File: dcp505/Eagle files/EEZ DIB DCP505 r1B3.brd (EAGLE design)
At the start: 160 x 95 mm, 328 parts, among them IC1 LP2951, IC10 OPA4197IDR, IC11 MC33272ADR2G, IC12 MC33274ADR2G, IC13 74HC4066PW, IC14 74AUP1G74DC.125, IC15 MCP23S17-E/SS, IC16 REF5025AIDR, IC17 DAC8552IDGKR, IC18 SN74LVC1G3157DCKR, IC19 ADS1120IPWR, IC2 SI8641BB-B-IS1, IC20 LM339D, IC21 LM211PWR, IC3 SN74LVC1G139DCUR, IC4 MC79L05, IC5 SI8641BB-B-IS1, IC6 AT24C04D-SSHM-T, IC7 TMP1075AIDGK, IC8 TL072D, IC9 MC33274ADR2G, J1 FCR7350R, J2 FCR7350B, K1 G6K-2F-5DC, Q1 IRFP250MPBF, Q10 MMBT5551, Q11 PSMN0R9-25YLC, Q12 PSMN0R9-25YLC, Q13 PSMN0R9-25YLC, Q14 2N7002, Q15 2N7002, Q16 MMBT5401, Q17 MMBT5401, Q18 2N7002, Q19 BSS84P, Q2 BCP56-16.115, Q20 BTA26-600, Q21 2N7002, Q22 MMBT5551, Q23 2N7002, Q24 2N7002, Q25 MMBT5551, Q26 MMBT5551, Q27 MMBT5401, Q28 MMBT5551, Q29 MMBT5551, Q3 BC856C, Q30 BSS84P, Q31 2N7002, Q4 BCP56-16.115, Q5 STF10P6F6, Q6 BCP56-16.115, Q7 MMBT5401, Q8 MMBT5401, Q9 MMBT5551, X1 ZL263-26DG, X2 22-05-7085, X3 39-30-3035, X4 1844249, X5 ZL263-20DG

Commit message: #26, #28, #29
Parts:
- added C76: 10n, rcl:C0805
- added Q32: 2N7002, EEZ_Lib1:SOT103P240X110-3N
- added R139: 10K, rcl:R0805
- added R140: 470R, rcl:R0805
- added R141: 100K, rcl:R0805
- C11: value 470n -> 100n; device rcl:C0805 -> rcl:C0603
- C43: value 10n -> 47n; device rcl:C0603 -> rcl:C0805
- C44: device rcl:C0603 -> rcl:C0805
- C45: value 100n -> 10n; device rcl:C0603 -> rcl:C0805
- C47, C59, C61, C63: value 1u -> 100n; device rcl:C0805 -> rcl:C0603
- C48: value 10u -> 1u; device rcl:C1206 -> rcl:C0805
- C49: value 100n -> 10u; device rcl:C0603 -> rcl:C1206
- C50: value 4u7 -> 100n; device EEZ_Lib1:EC1206 -> rcl:C0603
- C51: value 1u -> 4u7; device rcl:C0805 -> EEZ_Lib1:EC1206
- C52, C60, C62, C64: value 100n -> 1u; device rcl:C0603 -> rcl:C0805
- C53: value 3n3 -> 100n; device rcl:C0805 -> rcl:C0603
- C55: value 10n -> 3n3
- C56: value 3n3 -> 10n
- C58: value 100n -> 3n3; device rcl:C0603 -> rcl:C0805
- C66, C68: value N.C. -> 100n; device rcl:C0805 -> rcl:C0603
- C67: value 100n -> 1n; device rcl:C0603 -> rcl:C0805
- C69: value 10n -> 1n
- C70: value 10n/200V -> 10n; device rcl:C1206 -> rcl:C0805
- C71: value 2n2 -> 10n/200V; device rcl:C0805 -> rcl:C1206
- C72: value 470n -> 2n2; device rcl:C1206 -> rcl:C0805
- C73: value HHXC630ARA330MHA0G -> 470n; device EEZ_Lib1:CAPAE830X1050N -> rcl:C1206
- C74: value 10n/200V -> HHXC630ARA330MHA0G; device rcl:C1206 -> EEZ_Lib1:CAPAE830X1050N
- C75: value 10n -> 10n/200V; device rcl:C0805 -> rcl:C1206
- IC8: value TL072D -> MC33272ADR2G
- Q22: value MMBT5551 -> FMMT493TA
- Q25: value MMBT5551 -> 2N7002; device transistor:SOT23-BEC -> EEZ_Lib1:SOT103P240X110-3N
- Q27: value MMBT5401 -> MMBT5551
- Q28: value MMBT5551 -> MMBT5401
- Q30: value BSS84P -> MMBT5551; device EEZ_Lib1:SOT95P237X112-3N -> transistor:SOT23-BEC
- Q31: value 2N7002 -> BSS84P; device EEZ_Lib1:SOT103P240X110-3N -> EEZ_Lib1:SOT95P237X112-3N
- R100: value 10R -> 220R
- R101: value 10K -> 220R
- R102: value 10K -> 10R
- R103: value 470R -> 10K
- R104: value 5K1 -> 10K
- R105: value 47K -> 470R
- R106, R120: value 5K6 -> 5K1
- R107: value 330R -> 47K
- R108: value 750R -> 5K6
- R109, R114: value 1K -> 330R
- R110: value AC01000001007JA100 -> 750R; device rcl:0411/15 -> rcl:R0805
- R111: value 2K2 -> 1K
- R112: value 330R -> AC01000001007JA100; device rcl:R0805 -> rcl:0411/15
- R113: value 10K -> 2K2
- R116: value 6R8 -> 10K
- R117, R93: value 10K -> 100K
- R118: value 5K1 -> 6R2
- R122: value 1K -> 4K7
- R123: value 330R -> 5K6
- R124, R133: value 47K -> 10K
- R125: value 47K -> 1K
- R126: value 750R -> 330R
- R127: value 1K -> 47K
- R128: value 2K2 -> 47K
- R129: value 10K -> 750R
- R130, R77, R79, R84: value 10K -> 1K
- R131: value 1R -> 2K2
- R132: value 750R -> 10K
- R134: value 330R -> 1R
- R135: value 470R -> 750R
- R136: value 10K -> 47K
- R137: value 470R -> 330R
- R138: value 100K -> 470R
- R3: value 82K -> 86K6
- R59, R70: value 499K 0.1% -> 10K; device rcl:R0603 -> rcl:R0805
- R60: value 10K -> 1R
- R61: value 1R -> 0R1; device rcl:R0805 -> rcl:R1206
- R62: value 0R1 -> 0R010; device rcl:R1206 -> EEZ_Lib1:R_H2728
- R63: value 0R010 -> 10K; device EEZ_Lib1:R_H2728 -> rcl:R0805
- R64, R74: value 10K -> 499K 0.1%; device rcl:R0805 -> rcl:R0603
- R65: value 1K 0.1% -> 1K; device rcl:R0603 -> rcl:R0805
- R68: value 1K -> 40K2 0.1%; device rcl:R0805 -> rcl:R0603
- R69: value 40K2 0.1% -> 10K; device rcl:R0603 -> rcl:R0805
- R72: value 10K -> 0R010; device rcl:R0805 -> EEZ_Lib1:R_H2728
- R73: value 0R010 -> 1K 0.1%; device EEZ_Lib1:R_H2728 -> rcl:R0603
- R75, R81: value 100R -> 10K
- R76, R86: value 1K -> 1M
- R78, R82: value 1K -> 100R
- R88: value 100K -> 1K
- R89: value 270R -> 10K
- R90: value 47K -> 100K
- R91: value 100K -> 270R
- R92: value 470R -> 47K
- R94, R98, R99: value 220R -> 470R
- R95: value 220R -> 10K
- R96, R97: value 470R -> 220R
- moved R107 151.5 mm to (154.1, 27.2), turned to 90 degrees
- moved R136 134.0 mm to (23.0, 71.8), turned to 180 degrees
- moved Q30 133.1 mm to (23.0, 62.7), turned to 180 degrees
- moved R123 131.9 mm to (149.4, 14.3), turned to 180 degrees
- moved R124 130.7 mm to (150.2, 27.2), turned to 270 degrees
- moved Q31 126.4 mm to (142.4, 3.94), turned to 270 degrees
- moved R92 124.7 mm to (129.7, 33.5), turned to 0 degrees
- moved R91 113.3 mm to (12.8, 31.8), turned to 90 degrees
- moved R94 111.3 mm to (12.5, 76.3), turned to 180 degrees
- moved R98 110.6 mm to (11.8, 69.5), turned to 270 degrees
- moved R103 110.3 mm to (156.1, 27.2)
- moved R89 110.3 mm to (107.1, 89.0), turned to 270 degrees
- moved R96 108.9 mm to (110.7, 23.9), turned to 0 degrees
- moved R105 108.4 mm to (47.4, 45.9), turned to 270 degrees
- moved R97 105.9 mm to (110.7, 27.9), turned to 0 degrees
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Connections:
- new net !OVP_FAULT: D23.C, IC15.25, Q25.3, R122.2
- net !DP_DRIVE: now also R95.1; no longer R93.1
- net !FAULT_OUT: now also Q31.2, R89.2; no longer Q30.2, R87.2
- net !OVP_EN: now also Q26.B; no longer Q25.B
- net !SET_DP: now also R93.2; no longer R91.2
- net +5V: now also C46.1, C47.2, C60.2, R106.2, R120.2, R132.2, R138.2, R139.1, R89.1, R93.1; no longer C45.1, C46.2, C58.2, R104.2, R118.2, R129.2, R135.2, R136.1, R87.1, R91.1
- net +VREF: now also C51.+, C53.2, C63.2, R81.2, R87.2; no longer C50.+, C52.2, C62.2, R78.2, R85.2
- net AUX_IN: now also C56.2, R98.1; no longer C55.2, R96.1
- net AUX_USET_SW: now also R92.2; no longer R90.2
- net CC_ACTIVE: now also R120.1, R123.2; no longer R118.1, R120.2
- net CC_LED: now also R114.2; no longer R112.2
- net CV_ACTIVE: now also R106.1, R108.2; no longer R104.1, R106.2
- net CV_LED: now also R109.1; no longer R107.1
- net DP_LED: now also R95.2; no longer R93.2
- net GND: now also C46.2, C47.1, C49.2, C50.1, C51.-, C52.2, C56.1, C57.2, C63.1, C64.2, C69.1, Q25.2, Q27.E, Q29.E, Q31.3, Q32.2, R113.1, R115.2, R116.2, R117.1, R118.1, R119.2, R125.2, R127.1, R136.1, R141.1, R68.1, R71.1, R74.2, R91.2, R94.1; no longer C45.2, C46.1, C47.2, C49.1, C50.-, C51.2, C52.1, C56.2, C57.1, C63.2, C64.1, Q26.E, Q28.E, Q30.3, Q31.2, R111.1, R113.2, R114.2, R115.1, R116.1, R117.2, R122.2, R124.1, R133.1, R138.1, R69.1, R70.2, R72.1, R86.1, R89.2
- net ISENSE-: now also R68.2; no longer R69.2
- net I_CTRL: now also R59.2; no longer R60.2
- net I_MON: now also R101.1; no longer R99.1
- net I_SERVO: now also R124.1; no longer R121.1
- net I_SET: now also R96.1; no longer R94.1
- net N$1: now also R67.2, R72.2S; no longer R65.2, R73.2S
- net N$105: now also R108.1; no longer R106.1
- net N$106: now also R123.1; no longer R120.1
- net N$107: now also C70.2, Q28.B, R126.1, R129.2, R131.2; no longer C69.2, Q27.B, R123.1, R126.2, R128.2
- net N$108: now also C72.2, Q28.C, R128.1, R133.2; no longer C71.2, Q27.C, R125.1, R130.2
- net N$109: now also Q30.C, R130.1; no longer Q29.C, R127.1
- net N$110: now also C76.1, Q30.B, R135.1, R137.2; no longer C75.1, Q29.B, R132.1, R134.2
- net N$111: now also C72.1, Q27.B, R127.2, R128.2; no longer C71.1, Q26.B, R124.2, R125.2
- net N$112: now also Q29.B, R133.1, R136.2; no longer Q28.B, R130.1, R133.2
- net N$113: now also C73.2, R134.2; no longer C72.2, R131.2
- net N$114: now also Q32.3, R140.1; no longer Q31.3, R137.1
- net N$118: now also R109.2; no longer R107.2
- net N$12: now also R91.1; no longer R89.1
- net N$120: now also R140.2; no longer R137.2
- net N$121: now also R94.2; no longer R92.2
- net N$14: now also Q31.1, R139.2; no longer Q30.1, R136.2
- net N$15: now also R112.2; no longer R110.2
- net N$153: now also R103.2; no longer R101.2
- net N$161: now also R124.2; no longer R121.2
- net N$17: now also R98.2, R99.1; no longer R96.2, R97.1
- net N$170: now also R107.1, R113.2; no longer R105.1, R111.2
- net N$173: now also R130.2, R131.1; no longer R127.2, R128.1
- net N$177: now also R119.1, R121.2; no longer R117.1, R119.2
- net N$18: now also R105.1; no longer R103.1
- net N$19: now also R118.2; no longer R116.2
- net N$21: now also R111.1, R117.2; no longer R109.1, R115.2
- net N$23: now also R85.2, R87.1; no longer R83.2, R85.1
- net N$24: now also Q26.C; no longer Q25.C
- net N$25: now also R138.1; no longer R135.1
- net N$28: now also C43.1, R64.2, R67.1; no longer R59.2, R65.1
- net N$29: now also R62.2; no longer R63.2
- net N$30: now also Q26.E, R125.1; no longer Q25.E, R122.1
- net N$31: now also C67.2, R104.2; no longer C66.2, R102.2
- net N$32: now also R99.2; no longer R97.2
- net N$33: now also C69.2, R110.2, R115.1; no longer C68.2, R108.2, R113.1
- net N$35: now also C43.2, R64.1, R69.2; no longer R59.1, R74.2
- net N$37: now also C44.2, R76.1; no longer C43.2
- net N$4: now also C71.1, C73.1, C74.+, Q28.E, R126.2; no longer C69.1, C72.1, C73.+, Q27.E, R123.2
- net N$40: now also R63.1; no longer R64.1
- net N$41: now also R59.1, R63.2; no longer R60.1, R64.2
- net N$42: now also R79.1, R84.2; no longer R78.1, R82.2
- net N$43: now also C45.2, R65.2, R86.1; no longer C44.2, R68.2
- net N$44: now also R70.1, R71.2; no longer R71.1, R72.2
- net N$45: now also R90.2; no longer R88.2
- net N$46: now also R114.1; no longer R112.1
- net N$47: now also R84.1, R88.2; no longer R82.1, R86.2
- net N$48: now also R82.2, R85.1; no longer R81.2, R83.1
- net N$50: now also R72.1S, R73.2; no longer R67.2, R73.1S
- net N$51: now also R62.1S; no longer R63.1S
- net N$52: now also R77.2, R81.1; no longer R76.2, R79.1
- net N$53: now also R77.1, R78.2; no longer R75.2, R76.1
- net N$54: now also R73.1, R74.1; no longer R67.1, R70.1
- net N$56: now also R61.2; no longer R62.2
- net N$57: now also R69.1; no longer R74.1
- net N$58: now also R75.2, R78.1; no longer R75.1, R77.2
- net N$59: now also R62.2S; no longer R63.2S
- net N$62: now also R82.1, R83.2; no longer R81.1, R84.2
- net N$63: now also R60.1; no longer R61.1
- net N$65: now also C44.1, R75.1, R76.2; no longer C43.1, R77.1
- net N$67: now also C45.1, R83.1, R86.2; no longer C44.1, R84.1
- net N$7: now also D15.C, R60.2, R61.1, R72.2; no longer R61.2, R63.1, R73.2
- net N$70: now also C62.2, R102.2; no longer C60.2, R100.2
- net N$71: now also C52.1; no longer C51.1
- net N$72: now also C54.2, R96.2; no longer C53.2, R94.2
- net N$73: now also C58.2, R100.2; no longer C57.2, R98.2
- net N$74: now also R65.1; no longer R68.1
- net N$8: now also R70.2; no longer R71.2
- net N$80: now also C55.2, R97.2; no longer C54.2, R95.2
- net N$81: now also C57.1, R101.2; no longer C56.1, R99.2
- net OUTF+: now also R105.2; no longer R103.2
- net OVP_FAULT: now also Q25.1, R111.2, R116.1; no longer IC15.25, R109.2, R114.1
- net PE: now also C71.2, C75.1; no longer C70.2, C74.1
- net POST_OUT-: now also C74.-, C76.2, Q30.E, R137.1; no longer C73.-, C74.2, Q29.E, R131.1
- net PREG_OUT-: now also R112.1, R72.1; no longer D15.C, R110.1, R73.1
- net PWRGOOD: no longer D23.C
- net RSENSE: now also Q32.1, R141.2; no longer Q31.1, R138.2
- net SENSE+: now also R129.1; no longer R126.1
- net SENSE-: now also R135.2; no longer R132.2
- net SENSE_ERR: now also Q29.C, R132.1; no longer Q28.C, R129.1
- net SENSE_PROT: now also Q27.C; no longer Q26.C
- net U_MON: now also R100.1, R110.1; no longer R108.1, R98.1
- net U_SERVO: now also R103.1; no longer R101.1
- net U_SET: now also R104.1, R97.1; no longer R102.1, R95.1
- net V+: now also C49.1, C50.2, C64.1, C66.2, IC12.4, R102.1, R107.2, R122.1; no longer C47.1, C49.2, C63.1, C64.2, IC12.11, R100.1, R105.2
- net V-: now also C68.2, IC12.11, R121.1; no longer C67.2, IC12.4, R119.1
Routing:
- net !OVP_FAULT: track 0.00 -> 105.0 mm, vias 0 -> 6
- net OVP_FAULT: track 116.3 -> 40.9 mm, vias 6 -> 2
- net PWRGOOD: track 94.6 -> 66.9 mm, vias 8 -> 6
- net POST_OUT-: track 227.9 -> 246.3 mm
- net V+: track 421.6 -> 426.5 mm, vias 25 -> 26
- net N$37: track 43.7 -> 47.7 mm
- net DP_S: track 13.5 -> 9.59 mm
- net +VREF: track 153.1 -> 156.9 mm
- net N$43: track 31.5 -> 34.7 mm
- net AUX_IN: track 93.7 -> 91.1 mm
- net GND: track 183.1 -> 180.6 mm
- net PREG_OUT-: track 524.8 -> 522.3 mm
- net SENSE_PROT: track 99.7 -> 102.1 mm, vias 2 -> 4
- net N$57: track 9.32 -> 6.91 mm
- net V-: track 284.1 -> 281.8 mm, vias 18 -> 16
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- added copper zone on layer 1, net DP_S
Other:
- board text added: "EEZ DIB DCP505 (02/2019 r1B3)"
- board text added: "EEZ DIB DCP505 (02/2019 r1B3) Project source code: github.com/eez-open/modular-psu"
- board text removed: "EEZ DIB DCP505 (01/2019 r1B2)"
- board text removed: "EEZ DIB DCP505 (01/2019 r1B2) Project source code: github.com/eez-open/modular-psu"

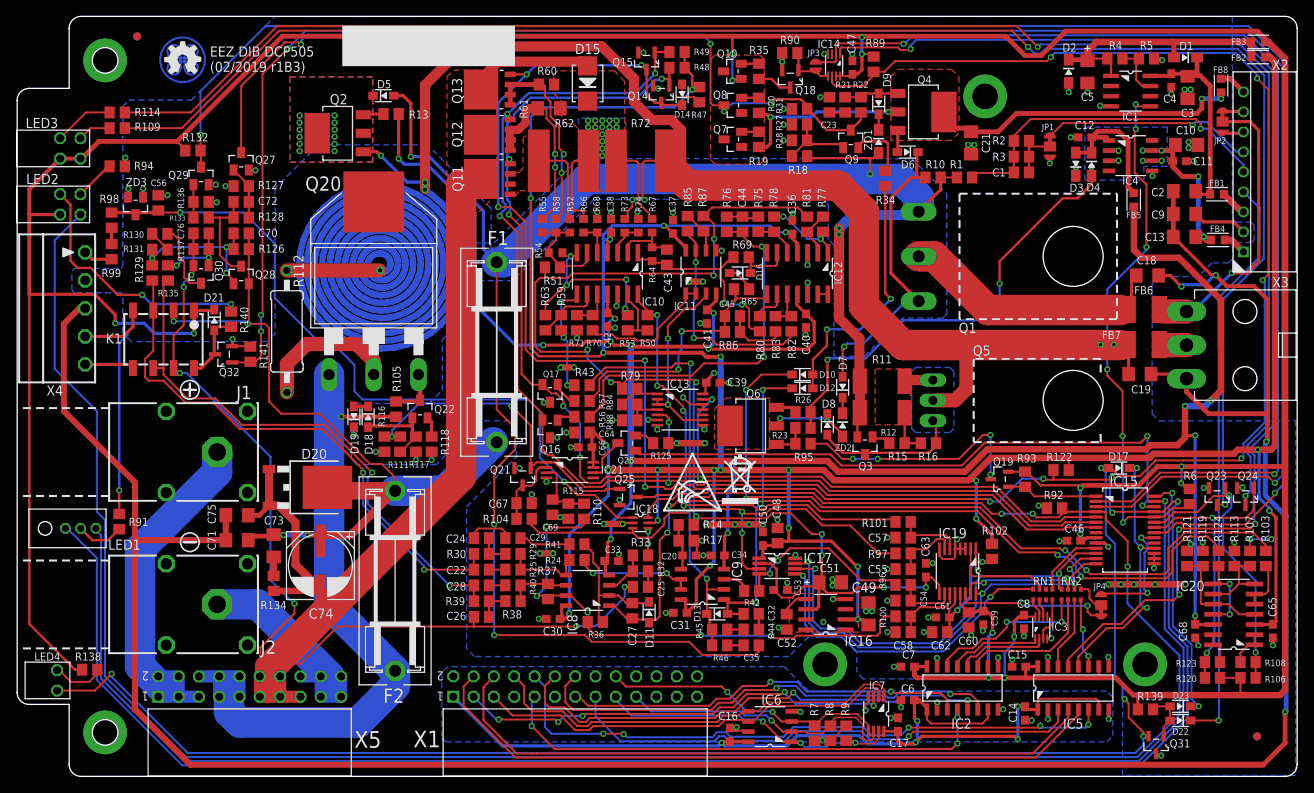
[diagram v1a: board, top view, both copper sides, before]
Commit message: DCP505 fault indication fix
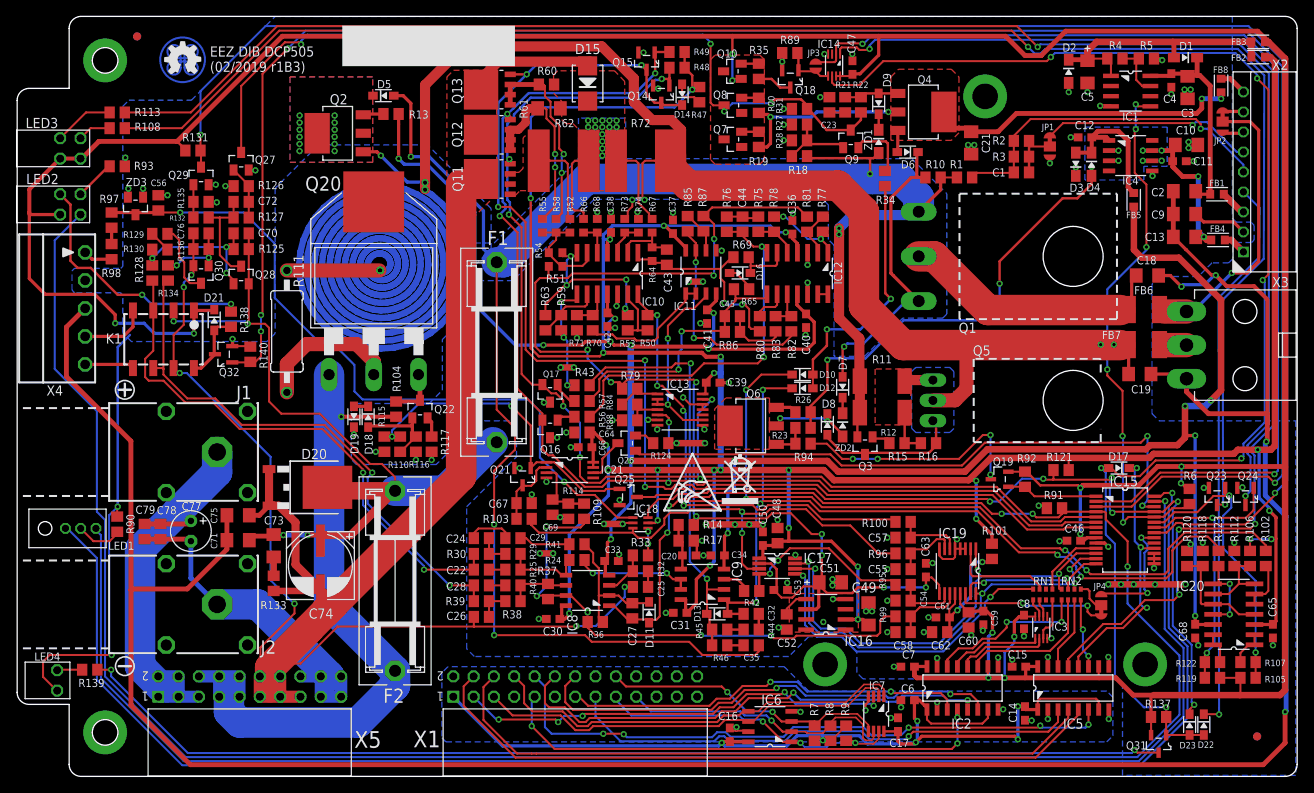
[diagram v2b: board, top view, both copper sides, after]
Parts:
- removed R141: 100K, rcl:R0805
- added C77: N.C., EEZ_Lib1:ECAP2/5
- added C78, C79: N.C., rcl:C0805
- R101: value 220R -> 10R
- R102: value 10R -> 10K
- R104, R139: value 10K -> 470R
- R105: value 470R -> 5K1
- R106: value 5K1 -> 47K
- R107: value 47K -> 5K6
- R108: value 5K6 -> 330R
- R109: value 330R -> 750R
- R110, R129: value 750R -> 1K
- R111: value 1K -> AC01000001007JA100; device rcl:R0805 -> rcl:0411/15
- R112: value AC01000001007JA100 -> 2K2; device rcl:0411/15 -> rcl:R0805
- R113: value 2K2 -> 330R
- R114, R137: value 330R -> 10K
- R116, R89: value 10K -> 100K
- R117: value 100K -> 6R2
- R118: value 6R2 -> 10K
- R119: value 10K -> 5K1
- R120: value 5K1 -> 10K
- R121: value 10K -> 4K7
- R122: value 4K7 -> 5K6
- R123: value 5K6 -> 10K
- R124: value 10K -> 1K
- R125: value 1K -> 330R
- R126: value 330R -> 47K
- R128: value 47K -> 750R
- R130: value 1K -> 2K2
- R131: value 2K2 -> 10K
- R133: value 10K -> 1R
- R134: value 1R -> 750R
- R135: value 750R -> 47K
- R136: value 47K -> 330R
- R140: value 470R -> 100K
- R3: value 86K6 -> 82K
- R51: device rcl:R0805 -> rcl:R0603
- R90: value 100K -> 270R
- R91: value 270R -> 47K
- R92: value 47K -> 100K
- R93: value 100K -> 470R
- R94: value 470R -> 10K
- R95: value 10K -> 220R
- R97: value 220R -> 470R
- R99: value 470R -> 220R
- moved R108 156.3 mm to (12.5, 81.0)
- moved R113 150.4 mm to (12.5, 83.0), turned to 180 degrees
- moved R137 133.2 mm to (142.7, 7.43)
- moved R139 132.0 mm to (9.08, 13.3)
- moved R112 121.8 mm to (152.1, 27.2)
- moved R93 120.0 mm to (12.5, 76.3), turned to 180 degrees
- moved R91 116.9 mm to (129.7, 33.5), turned to 0 degrees
- moved R105 111.7 mm to (153.9, 12.3), turned to 180 degrees
- moved R99 108.9 mm to (110.7, 20.0), turned to 0 degrees
- moved R97 107.3 mm to (11.8, 69.5), turned to 270 degrees
- moved R90 102.7 mm to (12.5, 31.5), turned to 90 degrees
- moved R118 97.4 mm to (148.2, 27.2)
- moved R103 92.8 mm to (63.4, 32.2), turned to 180 degrees
- moved R94 92.5 mm to (98.2, 41.6), turned to 0 degrees
- moved R109 75.5 mm to (70.9, 33.1), turned to 90 degrees
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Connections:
- net N$16 renamed U_CTRL+
- net N$27 renamed U_CTRL-
- removed net N$14: D22.A, D23.A, Q31.1, R139.2
- new net N$16: LED4.A, R139.1
- net !DP_DRIVE: now also R94.1; no longer R95.1
- net !FAULT_OUT: now also D22.A, D23.A, Q31.1, R137.2; no longer LED4.C, Q31.2, R89.2
- net !OVP_FAULT: now also R121.2; no longer R122.2
- net !SET_DP: now also R92.2; no longer R93.2
- net +5V: now also Q31.2, R105.2, R119.2, R131.2, R137.1, R92.1; no longer R106.2, R120.2, R132.2, R138.2, R139.1, R89.1, R93.1
- net AUX_IN: now also R97.1; no longer R98.1
- net AUX_USET_SW: now also R91.2; no longer R92.2
- net CC_ACTIVE: now also R119.1, R122.2; no longer R120.1, R123.2
- net CC_LED: now also R113.2; no longer R114.2
- net CV_ACTIVE: now also R105.1, R107.2; no longer R106.1, R108.2
- net CV_LED: now also R108.1; no longer R109.1
- net DP_LED: now also R94.2; no longer R95.2
- net GND: now also LED4.C, R112.1, R114.2, R116.1, R118.2, R124.2, R126.1, R135.1, R140.1, R89.1, R90.2, R91.1, R93.1; no longer Q31.3, R113.1, R116.2, R118.1, R119.2, R125.2, R127.1, R136.1, R141.1, R90.1, R91.2, R92.1, R94.1
- net I_MON: now also R100.1; no longer R101.1
- net I_SERVO: now also R123.1; no longer R124.1
- net I_SET: now also R95.1; no longer R96.1
- net N$105: now also R107.1; no longer R108.1
- net N$106: now also R122.1; no longer R123.1
- net N$107: now also R125.1, R128.2, R130.2; no longer R126.1, R129.2, R131.2
- net N$108: now also R127.1, R132.2; no longer R128.1, R133.2
- net N$109: now also R129.1; no longer R130.1
- net N$110: now also R134.1, R136.2; no longer R135.1, R137.2
- net N$111: now also R126.2; no longer R128.2
- net N$112: now also R132.1, R135.2; no longer R133.1, R136.2
- net N$113: now also R133.2; no longer R134.2
- net N$114: now also R138.1; no longer R140.1
- net N$118: now also R108.2; no longer R109.2
- net N$12: now also R90.1; no longer R91.1
- net N$120: now also R138.2; no longer R140.2
- net N$121: now also R93.2; no longer R94.2
- net N$15: now also R111.2; no longer R112.2
- net N$153: now also R102.2; no longer R103.2
- net N$161: now also R123.2; no longer R124.2
- net N$17: now also R97.2, R98.1; no longer R98.2, R99.1
- net N$170: now also R106.1, R112.2; no longer R107.1, R113.2
- net N$173: now also R129.2, R130.1; no longer R130.2, R131.1
- net N$177: now also R118.1, R120.2; no longer R119.1, R121.2
- net N$18: now also R104.1; no longer R105.1
- net N$19: now also R117.2; no longer R118.2
- net N$21: now also R110.1, R116.2; no longer R111.1, R117.2
- net N$25: now also Q31.3, R139.2; no longer LED4.A, R138.1
- net N$30: now also R124.1; no longer R125.1
- net N$31: now also R103.2; no longer R104.2
- net N$32: now also R98.2; no longer R99.2
- net N$33: now also R109.2, R114.1; no longer R110.2, R115.1
- net N$4: now also R125.2; no longer R126.2
- net N$45: now also R89.2; no longer R90.2
- net N$46: now also R113.1; no longer R114.1
- net N$70: now also R101.2; no longer R102.2
- net N$72: now also R95.2; no longer R96.2
- net N$73: now also R99.2; no longer R100.2
- net N$80: now also R96.2; no longer R97.2
- net N$81: now also R100.2; no longer R101.2
- net OUTC+: now also C77.+, C78.1, C79.1
- net OUTC-: now also C77.-, C78.2, C79.2
- net OUTF+: now also R104.2; no longer R105.2
- net OVP_FAULT: now also R110.2, R115.1; no longer R111.2, R116.1
- net POST_OUT-: now also R133.1, R136.1; no longer R134.1, R137.1
- net PREG_OUT-: now also R111.1; no longer R112.1
- net RSENSE: now also R140.2; no longer R141.2
- net SENSE+: now also R128.1; no longer R129.1
- net SENSE-: now also R134.2; no longer R135.2
- net SENSE_ERR: now also R131.1; no longer R132.1
- net U_MON: now also R109.1, R99.1; no longer R100.1, R110.1
- net U_SERVO: now also R102.1; no longer R103.1
- net U_SET: now also R103.1, R96.1; no longer R104.1, R97.1
- net V+: now also R101.1, R106.2, R121.1; no longer R102.1, R107.2, R122.1
- net V-: now also R120.1; no longer R121.1
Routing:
- net !FAULT_OUT: track 305.4 -> 169.0 mm, vias 8 -> 6
- net N$25: track 6.57 -> 137.7 mm, vias 0 -> 2
- net +5V: track 498.1 -> 449.9 mm, vias 14 -> 12
- net GND: track 180.6 -> 212.7 mm
- net OUTC-: track 29.0 -> 44.1 mm
- net OUTC+: track 47.0 -> 54.9 mm
- net N$14: track 6.36 -> 0.00 mm
- net PE: track 320.9 -> 324.1 mm
- net N$16: track 0.00 -> 3.16 mm
- net !FAULT: track 72.5 -> 70.2 mm
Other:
- board text added: "5 U_CTRL+"
- board text added: "6 U_CTRL-"
- board text removed: "5 U_MON+"
- board text removed: "6 U_MON-"
